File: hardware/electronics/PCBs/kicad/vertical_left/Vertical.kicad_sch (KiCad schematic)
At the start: 0 parts

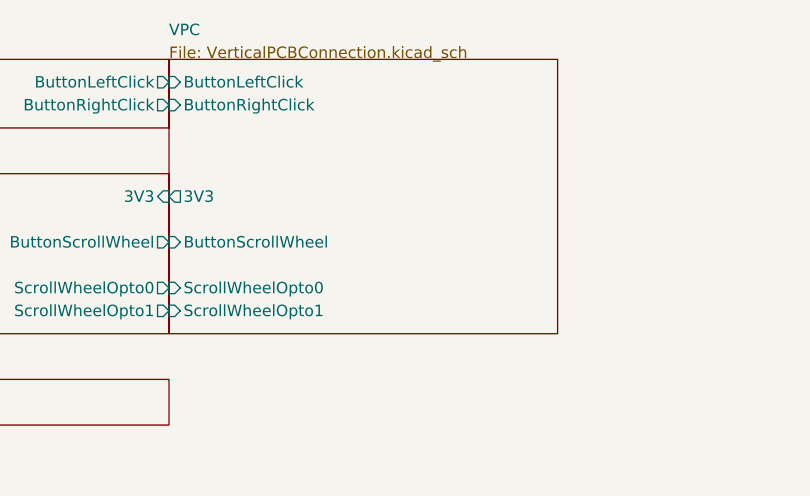
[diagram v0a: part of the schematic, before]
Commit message: Vertical portion flipped
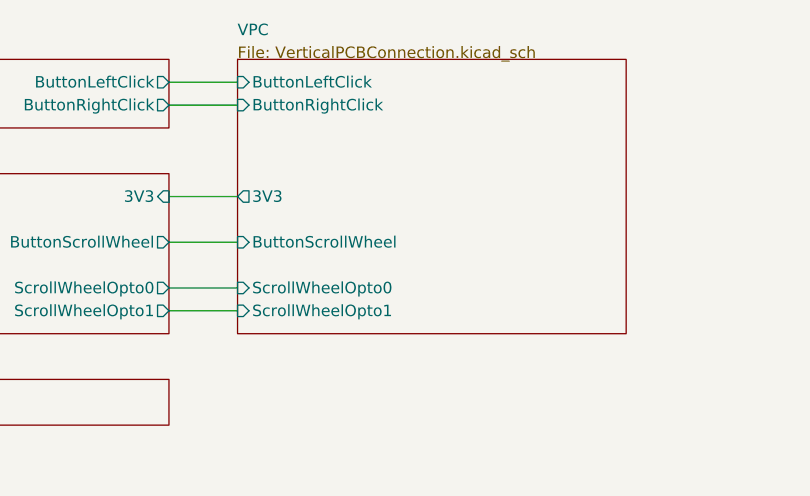
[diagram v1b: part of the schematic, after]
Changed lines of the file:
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@@
+		)
+	)
+	(wire
+		(pts
+			(xy 142.24 99.06) (xy 149.86 99.06)
+		)
+		(stroke
+			(width 0)
+			(type default)
+		)
+	)
+	(wire
+		(pts
+			(xy 142.24 109.22) (xy 149.86 109.22)
+		)
+		(stroke
+			(width 0)
+			(type default)
+		)
+	)
+	(wire
+		(pts
+			(xy 142.24 88.9) (xy 149.86 88.9)
+		)
+		(stroke
+			(width 0)
+			(type default)
 		)
 	)
@@
 		)
 	)
+	(wire
+		(pts
+			(xy 142.24 111.76) (xy 149.86 111.76)
+		)
+		(stroke
+			(width 0)
+			(type default)
+		)
+	)
 	(polyline
 		(pts
@@
 		)
 	)
+	(wire
+		(pts
+			(xy 142.24 86.36) (xy 149.86 86.36)
+		)
+		(stroke
+			(width 0)
+			(type default)
+		)
+	)
 	(polyline
 		(pts
@@
 			(type solid)
 			(color 0 0 0 1)
+		)
+	)
+	(wire
+		(pts
+			(xy 142.24 104.14) (xy 149.86 104.14)
+		)
+		(stroke
+			(width 0)
+			(type default)
 		)
 	)
@@
 	)
 	(sheet
-		(at 142.24 83.82)
+		(at 149.86 83.82)
 		(size 43.18 30.48)
 		(exclude_from_sim no)
@@
 		)
 		(property "Sheetname" "VPC"
-			(at 142.24 81.28 0)
+			(at 149.86 81.28 0)
 			(show_name no)
 			(do_not_autoplace no)
@@
 		)
 		(property "Sheetfile" "VerticalPCBConnection.kicad_sch"
-			(at 142.24 83.82 0)
+			(at 149.86 83.82 0)
 			(show_name no)
 			(do_not_autoplace no)
@@
 		)
 		(pin "3V3" output
-			(at 142.24 99.06 180)
+			(at 149.86 99.06 180)
 			(effects
 				(font
@@
 		)
 		(pin "ButtonRightClick" input
-			(at 142.24 88.9 180)
+			(at 149.86 88.9 180)
 			(effects
 				(font
@@
 		)
 		(pin "ButtonLeftClick" input
-			(at 142.24 86.36 180)
+			(at 149.86 86.36 180)
 			(effects
 				(font
@@
 		)
 		(pin "ScrollWheelOpto1" input
-			(at 142.24 111.76 180)
+			(at 149.86 111.76 180)
 			(effects
 				(font
@@
 		)
 		(pin "ScrollWheelOpto0" input
-			(at 142.24 109.22 180)
+			(at 149.86 109.22 180)
 			(effects
 				(font
@@
 		)
 		(pin "ButtonScrollWheel" input
-			(at 142.24 104.14 180)
+			(at 149.86 104.14 180)
 			(effects
 				(font
